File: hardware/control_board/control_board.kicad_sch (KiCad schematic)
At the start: 17 parts, among them J1 3V3, J2 24V, J3 Heatbed, J4 PWM, J5 Thermocouple, J6 SPI, Q1 IRLZ44N, U1 PC817, U2 MAX6675

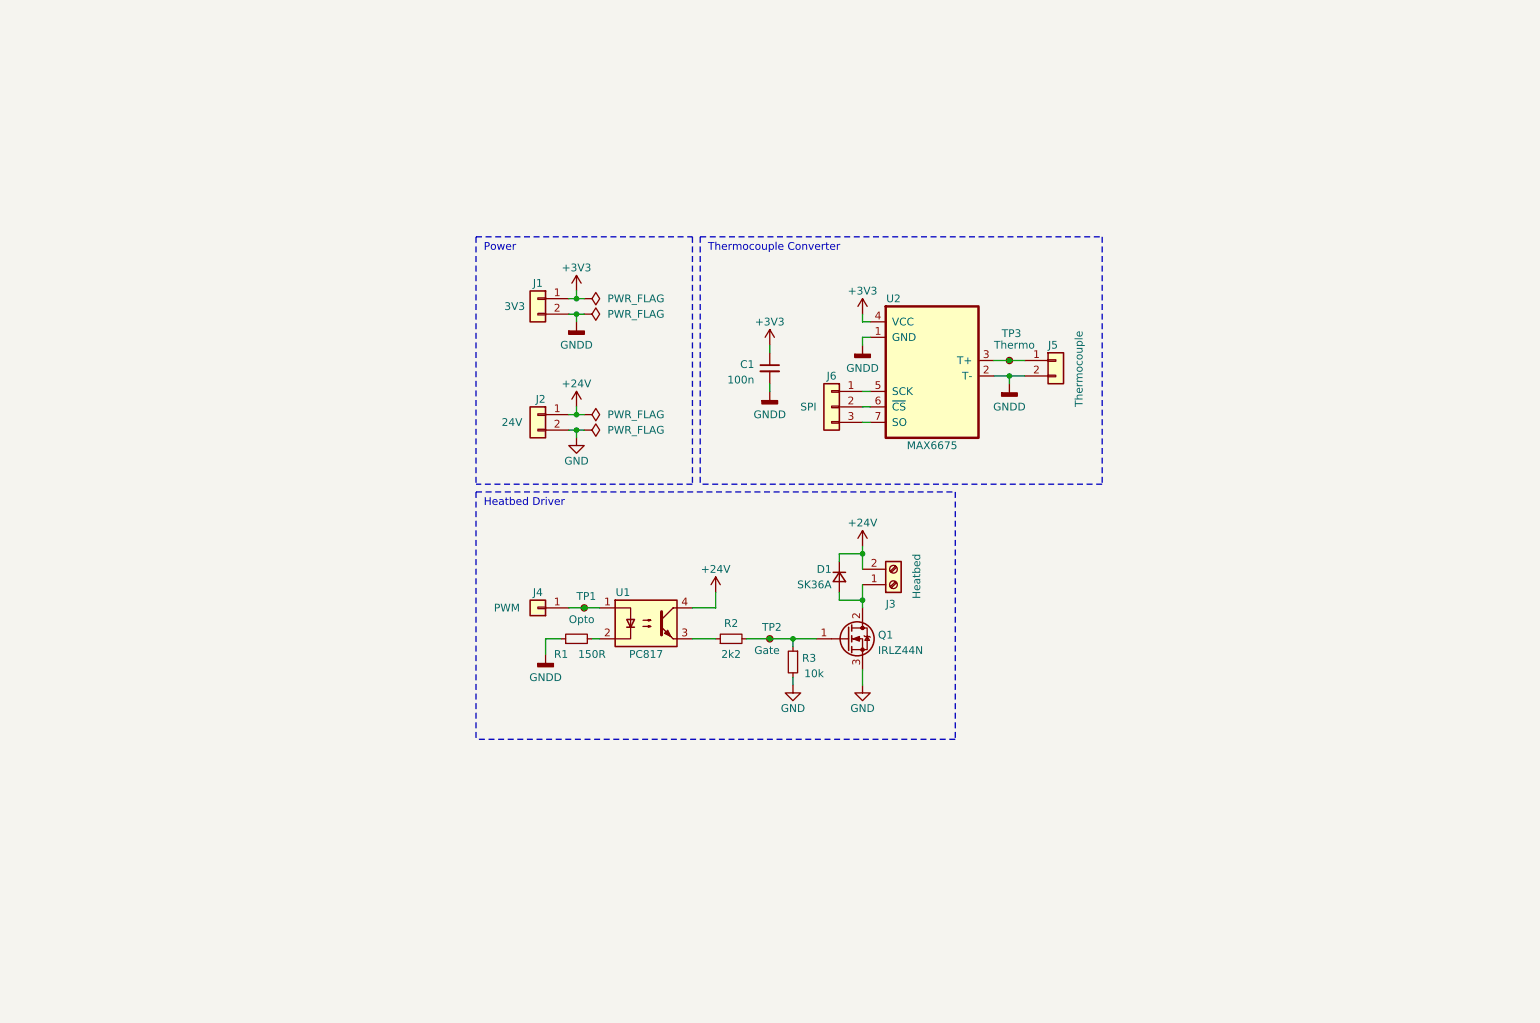
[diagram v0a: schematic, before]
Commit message: Use a dedicated MCU for the control board
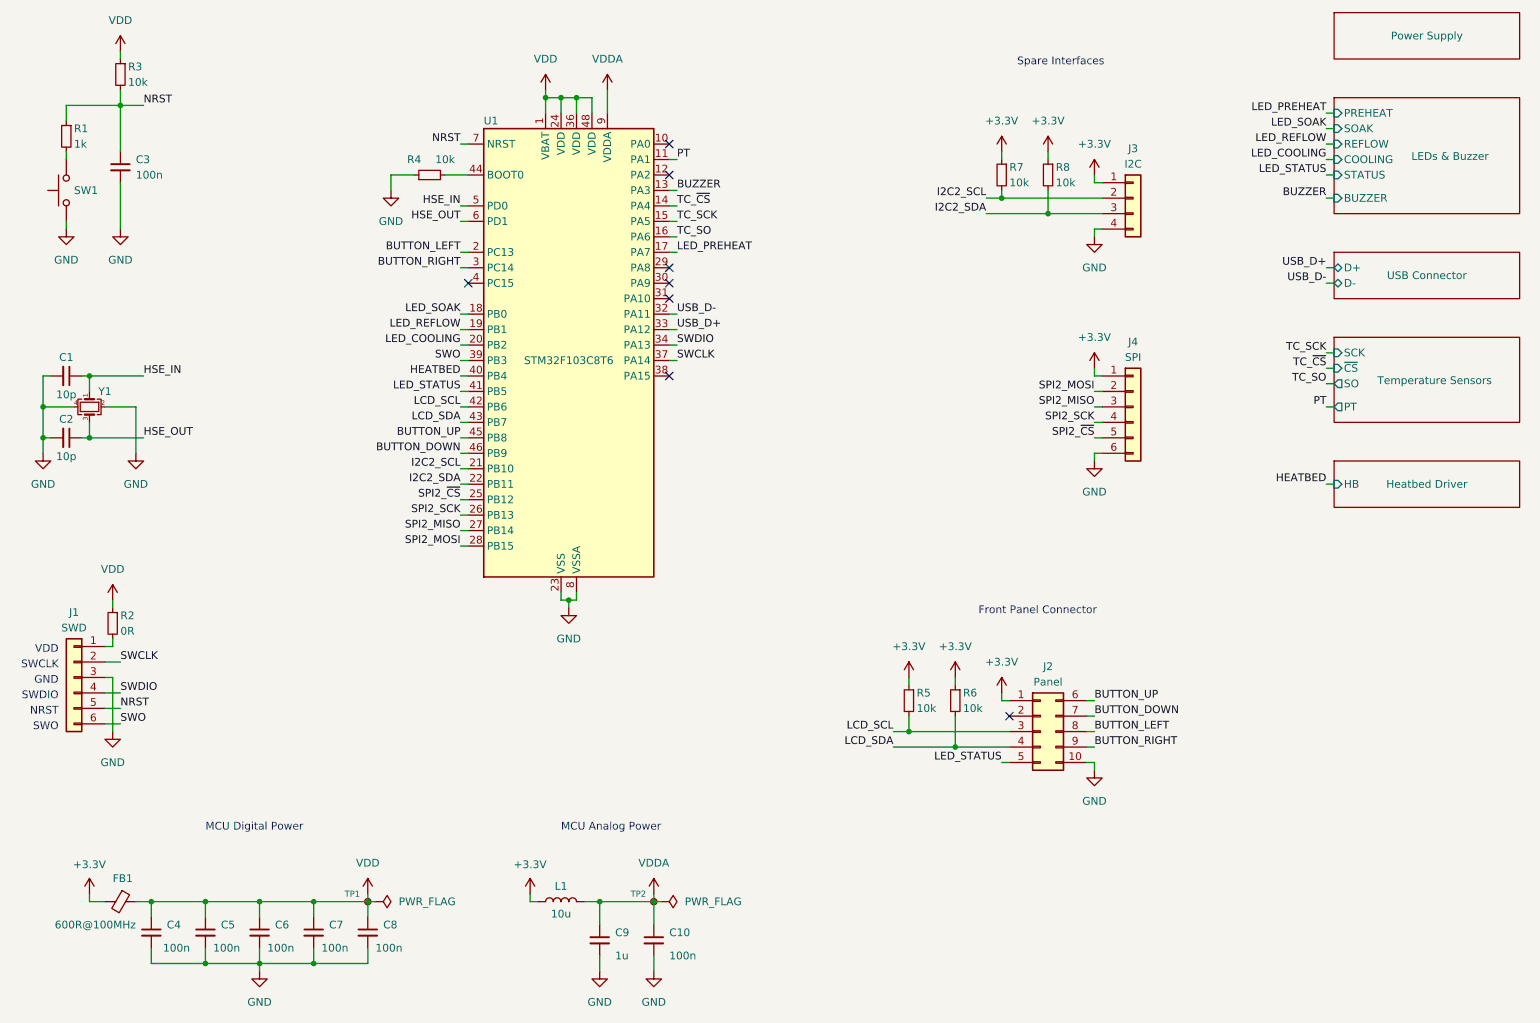
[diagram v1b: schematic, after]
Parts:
- removed D1: SK36A, Diode_SMD:D_SMA, symbol Device:D_Small
- removed J1: 3V3, Connector_PinHeader_2.54mm:PinHeader_1x02_P2.54mm_Vertical, symbol Connector_Generic:Conn_01x02
- removed J2: 24V, TerminalBlock:TerminalBlock_bornier-2_P5.08mm, symbol Connector_Generic:Conn_01x02
- removed J3: Heatbed, TerminalBlock:TerminalBlock_bornier-2_P5.08mm, symbol Connector:Screw_Terminal_01x02
- removed J4: PWM, Connector_PinHeader_2.54mm:PinHeader_1x01_P2.54mm_Vertical, symbol Connector_Generic:Conn_01x01
- removed J5: Thermocouple, Connector_PinHeader_2.54mm:PinHeader_1x02_P2.54mm_Vertical, symbol Connector_Generic:Conn_01x02
- removed J6: SPI, Connector_PinHeader_2.54mm:PinHeader_1x03_P2.54mm_Vertical, symbol Connector_Generic:Conn_01x03
- removed Q1: IRLZ44N, Package_TO_SOT_THT:TO-220-3_Vertical, symbol Transistor_FET:IRLZ44N
- removed TP3: Thermo, TestPoint:TestPoint_Pad_1.0x1.0mm, symbol Connector:TestPoint_Small
- removed U1: PC817, Package_SO:SSO-4_6.7x5.1mm_P2.54mm_Clearance8mm, symbol Isolator:PC817
- removed U2: MAX6675, Package_SO:SOIC-8_3.9x4.9mm_P1.27mm, symbol MAX6675:MAX6675
- added C10, C3, C4, C5, C6, C7, C8: 100n, Capacitor_SMD:C_0603_1608Metric, symbol Device:C_Small
- added C2: 10p, Capacitor_SMD:C_0603_1608Metric, symbol Device:C_Small
- added C9: 1u, Capacitor_SMD:C_0603_1608Metric, symbol Device:C_Small
- added FB1: 600R@100MHz, Inductor_SMD:L_0603_1608Metric, symbol Device:FerriteBead_Small
- added J1: SWD, Connector_PinHeader_2.54mm:PinHeader_1x06_P2.54mm_Vertical, symbol Connector_Generic:Conn_01x06
- added J2: Panel, Connector_PinHeader_2.54mm:PinHeader_2x05_P2.54mm_Vertical, symbol Connector_Generic:Conn_02x05_Top_Bottom
- added J3: I2C, symbol Connector_Generic:Conn_01x04
- added J4: SPI, symbol Connector_Generic:Conn_01x06
- added L1: 10u, Inductor_SMD:L_0603_1608Metric, symbol Device:L
- added R4, R5, R6, R7, R8: 10k, Resistor_SMD:R_0603_1608Metric, symbol Device:R_Small
- added SW1: B3U-1000PM, Button_Switch_SMD:SW_SPST_B3U-1000P, symbol Switch:SW_Push
- added U1: STM32F103C8T6, Package_QFP:LQFP-48_7x7mm_P0.5mm, symbol MCU_ST_STM32F1:STM32F103C8Tx
- added Y1: 8MHz, Crystal:Crystal_SMD_Abracon_ABM8G-4Pin_3.2x2.5mm, symbol Device:Crystal_GND24_Small
- C1: value 100n -> 10p
- R1: value 150R -> 1k
- R2: value 2k2 -> 0R
- TP1: value Opto -> TestPoint_Small; footprint TestPoint:TestPoint_Pad_1.0x1.0mm -> TestPoint:TestPoint_Pad_D1.0mm
- TP2: value Gate -> TestPoint_Small; footprint TestPoint:TestPoint_Pad_1.0x1.0mm -> TestPoint:TestPoint_Pad_D1.0mm
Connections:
- net GND: now also C1.2, C10.2, C2.2, C3.2, C4.2, C5.2, C6.2, C7.2, C8.2, C9.2, J1.3 (Pin_3), J2.10 (Pin_10), J3.4 (Pin_4), J4.6 (Pin_6), R4.1, SW1.1, U1.23 (VSS), U1.35 (VSS), U1.47 (VSS), U1.8 (VSSA), Y1.2, Y1.4; no longer R3.2
- net VDD: now reaches TP1.1
- net VDD: now also R2.1, R3.1, C4.1, C5.1, C6.1, C7.1, C8.1, FB1.1, U1.1 (VBAT), U1.24 (VDD), U1.36 (VDD), U1.48 (VDD)
- net at R1.2: now also SW1.2
- net +3V3 renamed HSE_IN
- net HSE_IN: now also U1.5 (PD0), Y1.1
- net GNDD renamed NRST
- net NRST: now also R3.2, C3.1, J1.5 (Pin_5), U1.7 (NRST); no longer C1.2
- new net: R4.2, U1.44 (BOOT0)
- new net: J1.1 (Pin_1), R2.2
- new net +3.3V: FB1.2, J2.1 (Pin_1), J3.1 (Pin_1), J4.1 (Pin_1), L1.1, R5.1, R6.1, R7.1, R8.1
- new net BUTTON_DOWN: J2.7 (Pin_7), U1.46 (PB9)
- new net BUTTON_LEFT: J2.8 (Pin_8), U1.2 (PC13)
- new net BUTTON_RIGHT: J2.9 (Pin_9), U1.3 (PC14)
- new net BUTTON_UP: J2.6 (Pin_6), U1.45 (PB8)
- new net BUZZER: U1.13 (PA3)
- new net HEATBED: U1.40 (PB4)
- new net HSE_OUT: C2.1, U1.6 (PD1), Y1.3
- new net I2C2_SCL: J3.2 (Pin_2), R7.2, U1.21 (PB10)
- new net I2C2_SDA: J3.3 (Pin_3), R8.2, U1.22 (PB11)
- new net LCD_SCL: J2.3 (Pin_3), R5.2, U1.42 (PB6)
- new net LCD_SDA: J2.4 (Pin_4), R6.2, U1.43 (PB7)
- new net LED_COOLING: U1.20 (PB2)
- new net LED_PREHEAT: U1.17 (PA7)
- new net LED_REFLOW: U1.19 (PB1)
- new net LED_SOAK: U1.18 (PB0)
- new net LED_STATUS: J2.5 (Pin_5), U1.41 (PB5)
- new net PT: U1.11 (PA1)
- new net SPI2_MISO: J4.3 (Pin_3), U1.27 (PB14)
- new net SPI2_MOSI: J4.2 (Pin_2), U1.28 (PB15)
- new net SPI2_SCK: J4.4 (Pin_4), U1.26 (PB13)
- new net SPI2_~{CS}: J4.5 (Pin_5), U1.25 (PB12)
- new net SWCLK: J1.2 (Pin_2), U1.37 (PA14)
- new net SWDIO: J1.4 (Pin_4), U1.34 (PA13)
- new net SWO: J1.6 (Pin_6), U1.39 (PB3)
- new net TC_SCK: U1.15 (PA5)
- new net TC_SO: U1.16 (PA6)
- new net TC_~{CS}: U1.14 (PA4)
- new net USB_D+: U1.33 (PA12)
- new net USB_D-: U1.32 (PA11)
- new net VDDA: C10.1, C9.1, L1.2, TP2.1, U1.9 (VDDA)
- no-connect marks 0 -> 8
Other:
- added sheet Heatbed Driver (heatbed_driver.kicad_sch)
- added sheet LEDs & Buzzer (leds.kicad_sch)
- added sheet Power Supply (power_supply.kicad_sch)
- added sheet Temperature Sensors (temperature_sensors.kicad_sch)
- added sheet USB Connector (usb_connector.kicad_sch)
- note added: "Front Panel Connector"
- note added: "GND"
- note added: "MCU Analog Power"
- note added: "MCU Digital Power"
- note added: "NRST"
- note added: "SWCLK"
- note added: "SWDIO"
- note added: "SWO"
- note added: "Spare Interfaces"
- note added: "VDD"
- note removed: "Heatbed Driver"
- note removed: "Power"
- note removed: "Thermocouple Converter"
- company: I. Kajdan -> Author: I. Kajdan
- title: Reflow Hot-Plate Control Board -> Reflow Hot Plate Control Board

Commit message: Adjust component values
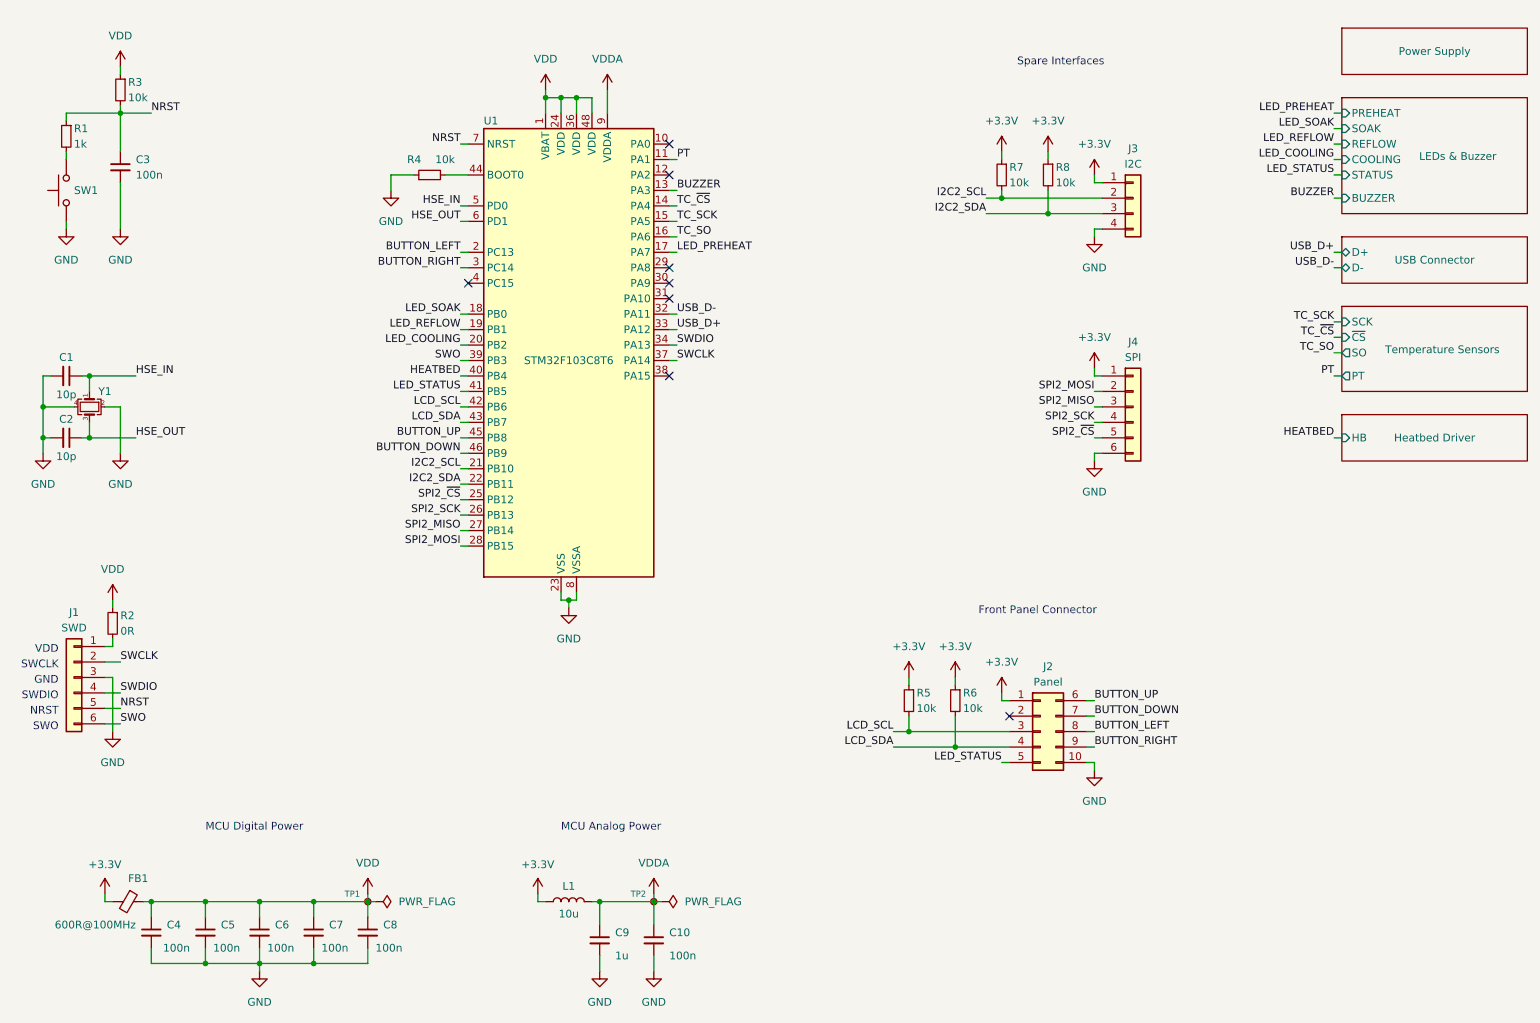
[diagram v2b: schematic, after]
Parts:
- J3: footprint (none) -> Connector_PinHeader_2.54mm:PinHeader_1x04_P2.54mm_Vertical
- J4: footprint (none) -> Connector_PinHeader_2.54mm:PinHeader_1x06_P2.54mm_Vertical
- Y1: footprint Crystal:Crystal_SMD_Abracon_ABM8G-4Pin_3.2x2.5mm -> Crystal:Crystal_SMD_3225-4Pin_3.2x2.5mm
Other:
- moved on the sheet: FB1, L1, R3

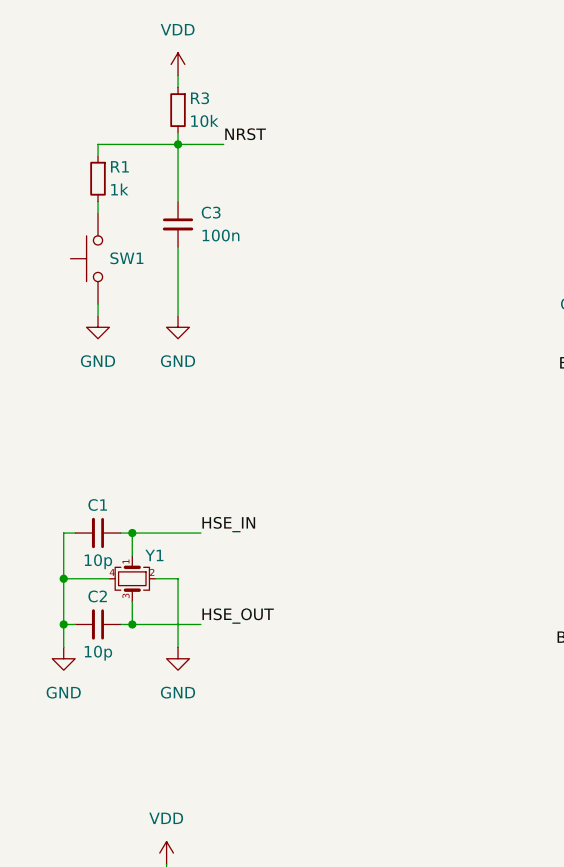
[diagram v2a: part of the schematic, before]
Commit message: Use a 3-wire RTD configuration
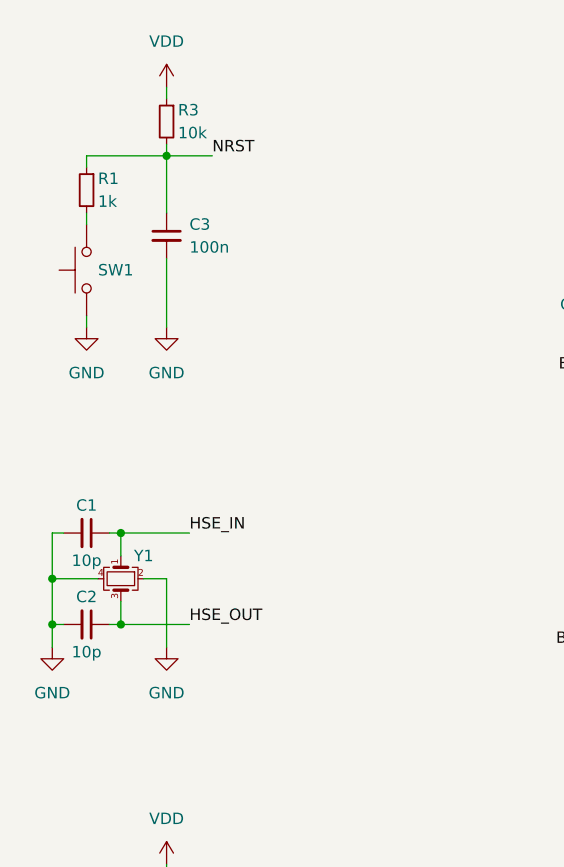
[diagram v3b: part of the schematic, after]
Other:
- moved on the sheet: C1, C2, C3, R1, R3, SW1, Y1

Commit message: Assign footprints to components
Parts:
- added TP5 (x2): TestPoint_Small, TestPoint:TestPoint_Pad_D1.0mm, symbol Connector:TestPoint_Small
- J2: footprint Connector_PinHeader_2.54mm:PinHeader_2x05_P2.54mm_Vertical -> Local_Library:52808-1070; symbol Connector_Generic:Conn_02x05_Top_Bottom -> Connector_Generic:Conn_01x10; Component (none) -> 52808-1070
- SW1: value B3U-1000PM -> Reset; Component (none) -> B3U-1000PM
- Y1: Component (none) -> ECS-80-18-33-JGN-TR
- renumbered R3 to R2, R2 to R3, R7 to R6, R6 to R7
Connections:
- net GND: now also J2.4 (Pin_4)
- net LCD_SCL: now also J2.2 (Pin_2), TP5.1; no longer J2.3 (Pin_3)
- net LCD_SDA: now also J2.3 (Pin_3), TP5.1; no longer J2.4 (Pin_4)
- no-connect marks 8 -> 7
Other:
- note added: "Additional Interfaces"
- note removed: "Spare Interfaces"
- moved on the sheet: C1, C10, C2, C3, C4, C5, C6, C7, C8, C9, FB1, J1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
